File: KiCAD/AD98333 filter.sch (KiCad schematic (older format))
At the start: 0 parts

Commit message: Add mcu
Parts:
- added FL?: EMI_Filter_LCL, symbol Device:EMI_Filter_LCL
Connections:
- new net GND: FL?.2
- new net IN_A_Out: FL?.3
- new net MClk_Fi: FL?.1
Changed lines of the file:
@@
 $Descr A4 11693 8268
 encoding utf-8
-Sheet 1 5
+Sheet 5 6
 Title "AM & FM Transceiver"
 Date ""
@@
 Comment4 ""
 $EndDescr
+Text Label 2850 1650 2    50   ~ 0
+MClk_Fi
+Text Label 4500 1650 0    50   ~ 0
+IN_A_Out
+$Comp
+L Device:EMI_Filter_LCL FL?
+U 1 1 5E7CF349
+P 3450 1750
+F 0 "FL?" H 3450 2067 50  0000 C CNN
+F 1 "EMI_Filter_LCL" H 3450 1976 50  0000 C CNN
+F 2 "" V 3450 1750 50  0001 C CNN
+F 3 "http://www.murata.com/~/media/webrenewal/support/library/catalog/products/emc/emifil/c31e.ashx?la=en-gb" V 3450 1750 50  0001 C CNN
+	1    3450 1750
+	1    0    0    -1
+$EndComp
+$Comp
+L power:GND #PWR?
+U 1 1 5E7CF8C3
+P 3450 2050
+F 0 "#PWR?" H 3450 1800 50  0001 C CNN
+F 1 "GND" H 3455 1877 50  0000 C CNN
+F 2 "" H 3450 2050 50  0001 C CNN
+F 3 "" H 3450 2050 50  0001 C CNN
+	1    3450 2050
+	1    0    0    -1
+$EndComp
+Wire Wire Line
+	3450 1850 3450 2050
+Wire Wire Line
+	2850 1650 3150 1650
+Wire Wire Line
+	3750 1650 4500 1650
 $EndSCHEMATC

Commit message: Just save files Begin PCB
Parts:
- FL1: renamed from FL?; footprint (none) -> Filter:Filter_Mini-Circuits_FV1206-7
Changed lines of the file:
@@
 $Descr A4 11693 8268
 encoding utf-8
-Sheet 5 5
+Sheet 4 4
 Title "AM & FM Transceiver"
 Date ""
@@
 IN_A_Out
 $Comp
-L Device:EMI_Filter_LCL FL?
+L Device:EMI_Filter_LCL FL1
 U 1 1 5E7CF349
 P 3450 1750
-F 0 "FL?" H 3450 2067 50  0000 C CNN
+F 0 "FL1" H 3450 2067 50  0000 C CNN
 F 1 "EMI_Filter_LCL" H 3450 1976 50  0000 C CNN
-F 2 "" V 3450 1750 50  0001 C CNN
+F 2 "Filter:Filter_Mini-Circuits_FV1206-7" V 3450 1750 50  0001 C CNN
 F 3 "http://www.murata.com/~/media/webrenewal/support/library/catalog/products/emc/emifil/c31e.ashx?la=en-gb" V 3450 1750 50  0001 C CNN
 	1    3450 1750
@@
 $EndComp
 $Comp
-L power:GND #PWR?
+L power:GND #PWR0128
 U 1 1 5E7CF8C3
 P 3450 2050
-F 0 "#PWR?" H 3450 1800 50  0001 C CNN
+F 0 "#PWR0128" H 3450 1800 50  0001 C CNN
 F 1 "GND" H 3455 1877 50  0000 C CNN
 F 2 "" H 3450 2050 50  0001 C CNN

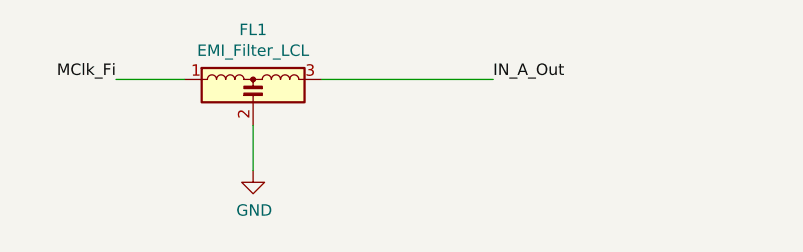
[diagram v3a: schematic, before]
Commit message: Make PCB and change NPN and PNP for AM output
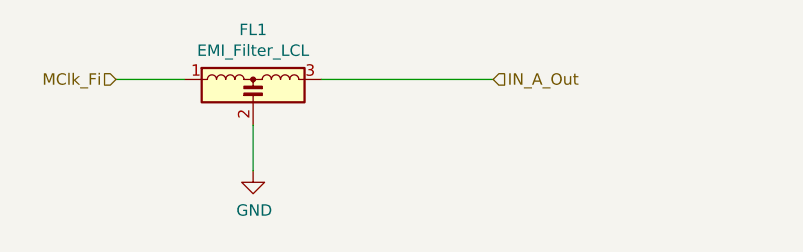
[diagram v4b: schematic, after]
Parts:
- FL1: footprint Filter:Filter_Mini-Circuits_FV1206-7 -> Ceramic_Filter:SFECK
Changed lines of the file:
@@
 $Descr A4 11693 8268
 encoding utf-8
-Sheet 4 4
+Sheet 3 4
 Title "AM & FM Transceiver"
 Date ""
@@
 Comment4 ""
 $EndDescr
-Text Label 2850 1650 2    50   ~ 0
-MClk_Fi
-Text Label 4500 1650 0    50   ~ 0
-IN_A_Out
 $Comp
 L Device:EMI_Filter_LCL FL1
@@
 F 0 "FL1" H 3450 2067 50  0000 C CNN
 F 1 "EMI_Filter_LCL" H 3450 1976 50  0000 C CNN
-F 2 "Filter:Filter_Mini-Circuits_FV1206-7" V 3450 1750 50  0001 C CNN
+F 2 "Ceramic_Filter:SFECK" V 3450 1750 50  0001 C CNN
 F 3 "http://www.murata.com/~/media/webrenewal/support/library/catalog/products/emc/emifil/c31e.ashx?la=en-gb" V 3450 1750 50  0001 C CNN
 	1    3450 1750
@@
 Wire Wire Line
 	3750 1650 4500 1650
+Text HLabel 2850 1650 0    50   Input ~ 0
+MClk_Fi
+Text HLabel 4500 1650 2    50   Input ~ 0
+IN_A_Out
 $EndSCHEMATC

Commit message: Schematics and PCB update
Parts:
- removed FL1: EMI_Filter_LCL, Ceramic_Filter:SFECK, symbol Device:EMI_Filter_LCL
- added C16, C17: 100n, Capacitor_SMD:C_0805_2012Metric, symbol Device:C
- added R19: R, Resistor_SMD:R_0805_2012Metric, symbol Device:R
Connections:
- net GND: now also C17.1
- net IN_A_Out: now also C16.2
- net MClk_Fi: now also R19.1
- new net: C16.1, C17.2, R19.2
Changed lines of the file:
@@
 Comment4 ""
 $EndDescr
+Text HLabel 5300 1650 2    50   Input ~ 0
+IN_A_Out
 $Comp
-L Device:EMI_Filter_LCL FL1
-U 1 1 5E7CF349
-P 3450 1750
-F 0 "FL1" H 3450 2067 50  0000 C CNN
-F 1 "EMI_Filter_LCL" H 3450 1976 50  0000 C CNN
-F 2 "Ceramic_Filter:SFECK" V 3450 1750 50  0001 C CNN
-F 3 "http://www.murata.com/~/media/webrenewal/support/library/catalog/products/emc/emifil/c31e.ashx?la=en-gb" V 3450 1750 50  0001 C CNN
-	1    3450 1750
-	1    0    0    -1
+L Device:C C?
+U 1 1 5E9AE17E
+P 4950 1650
+AR Path="/5E70F6BF/5E9AE17E" Ref="C?"  Part="1"
+AR Path="/5E9AE17E" Ref="C?"  Part="1"
+AR Path="/5E71DA61/5E9AE17E" Ref="C16"  Part="1"
+F 0 "C16" V 4698 1650 50  0000 C CNN
+F 1 "100n" V 4789 1650 50  0000 C CNN
+F 2 "Capacitor_SMD:C_0805_2012Metric" H 4988 1500 50  0001 C CNN
+F 3 "~" H 4950 1650 50  0001 C CNN
+	1    4950 1650
+	0    -1   -1   0
 $EndComp
 $Comp
-L power:GND #PWR0128
-U 1 1 5E7CF8C3
-P 3450 2050
-F 0 "#PWR0128" H 3450 1800 50  0001 C CNN
-F 1 "GND" H 3455 1877 50  0000 C CNN
-F 2 "" H 3450 2050 50  0001 C CNN
-F 3 "" H 3450 2050 50  0001 C CNN
-	1    3450 2050
+L Device:R R?
+U 1 1 5E9B32E8
+P 4050 1650
+AR Path="/5E9B32E8" Ref="R?"  Part="1"
+AR Path="/5E71DA61/5E9B32E8" Ref="R19"  Part="1"
+F 0 "R19" V 3843 1650 50  0000 C CNN
+F 1 "R" V 3934 1650 50  0000 C CNN
+F 2 "Resistor_SMD:R_0805_2012Metric" V 3980 1650 50  0001 C CNN
+F 3 "~" H 4050 1650 50  0001 C CNN
+	1    4050 1650
+	0    -1   -1   0
+$EndComp
+$Comp
+L power:GND #PWR0172
+U 1 1 5E9B3A78
+P 4450 2100
+F 0 "#PWR0172" H 4450 1850 50  0001 C CNN
+F 1 "GND" H 4455 1927 50  0000 C CNN
+F 2 "" H 4450 2100 50  0001 C CNN
+F 3 "" H 4450 2100 50  0001 C CNN
+	1    4450 2100
 	1    0    0    -1
 $EndComp
 Wire Wire Line
-	3450 1850 3450 2050
+	3750 1650 3900 1650
 Wire Wire Line
-	2850 1650 3150 1650
+	4200 1650 4450 1650
 Wire Wire Line
-	3750 1650 4500 1650
-Text HLabel 2850 1650 0    50   Input ~ 0
+	5100 1650 5300 1650
+Wire Wire Line
+	4450 1800 4450 1650
+Connection ~ 4450 1650
+Wire Wire Line
+	4450 1650 4800 1650
+$Comp
+L Device:C C?
+U 1 1 5E9B6BE3
+P 4450 1950
+AR Path="/5E70F6BF/5E9B6BE3" Ref="C?"  Part="1"
+AR Path="/5E9B6BE3" Ref="C?"  Part="1"
+AR Path="/5E71DA61/5E9B6BE3" Ref="C17"  Part="1"
+F 0 "C17" V 4198 1950 50  0000 C CNN
+F 1 "100n" V 4289 1950 50  0000 C CNN
+F 2 "Capacitor_SMD:C_0805_2012Metric" H 4488 1800 50  0001 C CNN
+F 3 "~" H 4450 1950 50  0001 C CNN
+	1    4450 1950
+	-1   0    0    1
+$EndComp
+Text HLabel 3750 1650 0    50   Input ~ 0
 MClk_Fi
-Text HLabel 4500 1650 2    50   Input ~ 0
-IN_A_Out
 $EndSCHEMATC
